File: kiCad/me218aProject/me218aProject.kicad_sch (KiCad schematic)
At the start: 23 parts, among them M1 Motor_Servo, M2 Motor_Servo, M3 Motor_Servo, M4 Motor_Servo, SW1 SW-PB, U1 PIC32MX170F256B, U2 74ACT244, U3 LED_Matrix, U4 USB2Serial

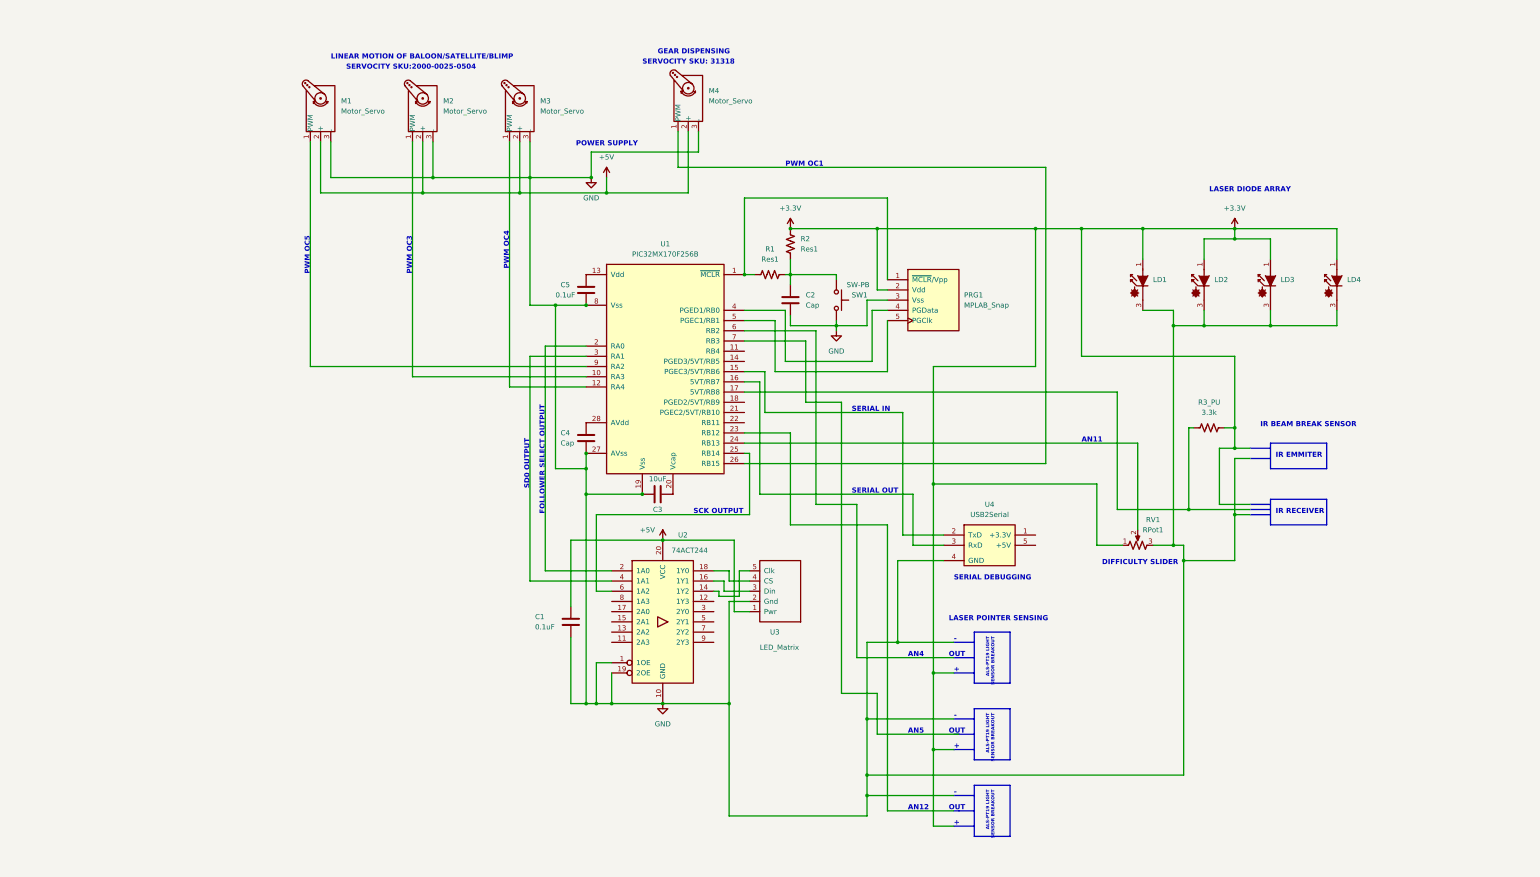
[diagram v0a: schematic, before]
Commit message: Update KiCad schematic and cleanup event checkerss and LED display routines
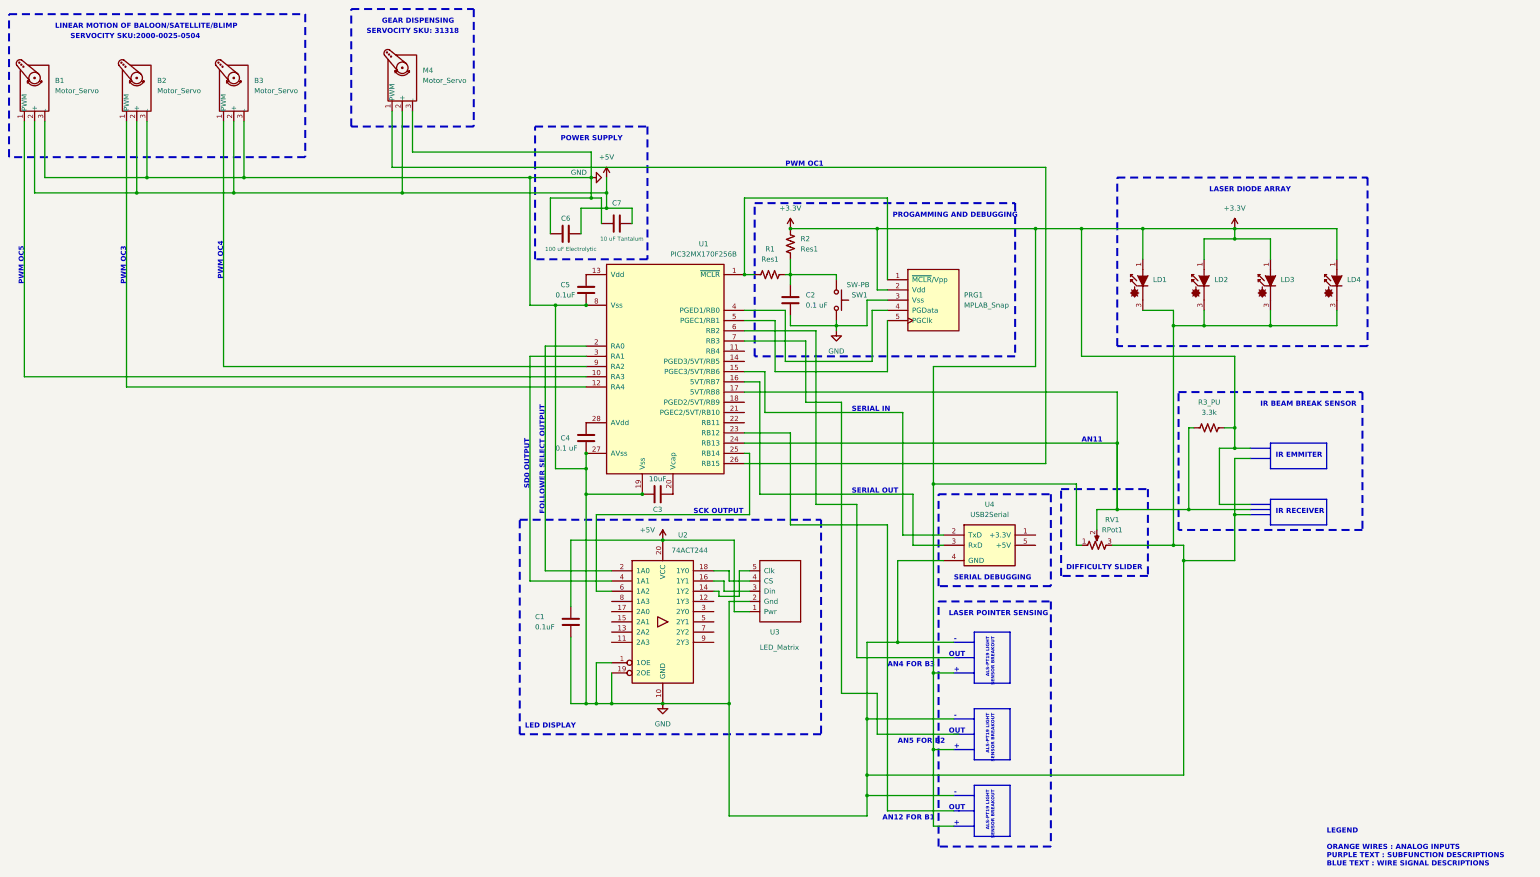
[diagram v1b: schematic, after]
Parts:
- added C6: 100 uF Electrolytic, symbol Device:C
- added C7: 10 uF Tantalum, symbol Device:C
- C2, C4: value Cap -> 0.1 uF
- renumbered M1 to B1, M2 to B2, M3 to B3
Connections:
- net +5V: now also C6.2, C7.2
- net GND: now also C6.1, C7.1
- net at B1.1 (PWM): now also U1.10 (RA3); no longer U1.9 (RA2)
- net at RV1.2, U1.24 (RB13): now also R3_PU.1, U1.17 (5VT/RB8)
- net at B2.1 (PWM): now also U1.12 (RA4); no longer U1.10 (RA3)
- net at B3.1 (PWM): now also U1.9 (RA2); no longer U1.12 (RA4)
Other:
- note added: "AN12 FOR B1"
- note added: "AN4 FOR B3"
- note added: "AN5 FOR B2"
- note added: "LED DISPLAY"
- note added: "LEGEND ORANGE WIRES : ANALOG INPUTS PURPLE TEXT : SUBFUNCTION DESCRIPTIONS BLUE TEXT : WIRE SIGNAL DESCRIPTIONS"
- note added: "PROGAMMING AND DEBUGGING"
- note removed: "AN12"
- note removed: "AN4"
- note removed: "AN5"
- moved on the sheet: B1, B2, B3, M4, RV1
